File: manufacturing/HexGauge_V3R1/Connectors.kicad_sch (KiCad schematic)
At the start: 14 parts, among them J1 USB_B_Micro, J3 Micro_SD_Card, J4 Conn_01x04_Pin, J5 Conn_02x05_Odd_Even, U4 USBLC6-4

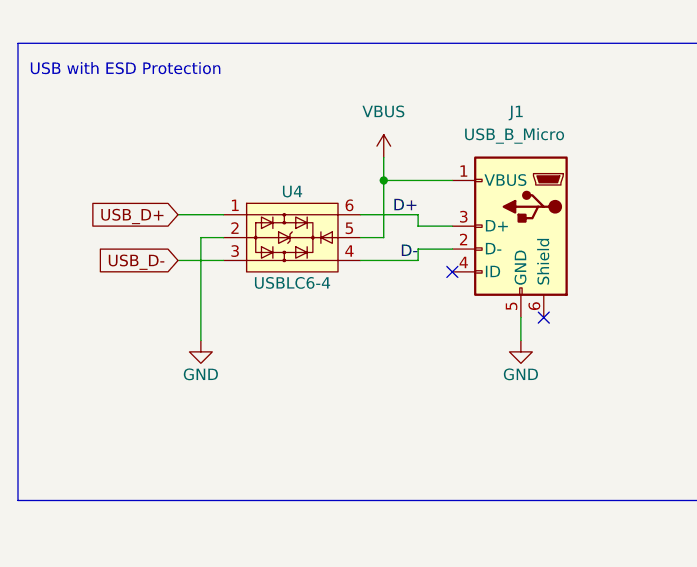
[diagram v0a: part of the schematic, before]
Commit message: Cost calculation
Find extended parts on mouser
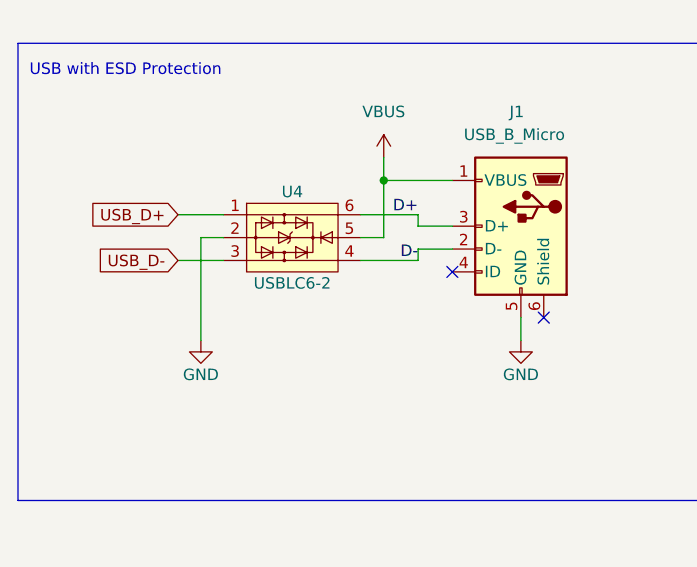
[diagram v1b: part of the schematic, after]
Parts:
- J5: footprint Connector_PinHeader_1.27mm:PinHeader_2x05_P1.27mm_Vertical_SMD -> Connector_PinHeader_1.27mm:PinHeader_2x05_P1.27mm_Vertical
- U4: value USBLC6-4 -> USBLC6-2; LCSC Part # C111212 -> C7519
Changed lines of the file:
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@@
       (effects (font (size 1.27 1.27)))
     )
-    (property "Footprint" "Connector_PinHeader_1.27mm:PinHeader_2x05_P1.27mm_Vertical_SMD" (at 137.16 63.5 0)
+    (property "Footprint" "Connector_PinHeader_1.27mm:PinHeader_2x05_P1.27mm_Vertical" (at 137.16 63.5 0)
       (effects (font (size 1.27 1.27)) hide)
     )
@@
     )
   )
+  (symbol (lib_id "Power_Protection:WE-TVS-82400102") (at 55.88 59.69 0) (unit 1)
+    (in_bom yes) (on_board yes) (dnp no)
+    (property "Reference" "U4" (at 55.88 54.61 0)
+      (effects (font (size 1.27 1.27)))
+    )
+    (property "Value" "USBLC6-2" (at 55.88 64.77 0)
+      (effects (font (size 1.27 1.27)))
+    )
+    (property "Footprint" "Package_TO_SOT_SMD:SOT-23-6" (at 55.88 64.77 0)
+      (effects (font (size 1.27 1.27)) hide)
+    )
+    (property "Datasheet" "https://www.st.com/resource/en/datasheet/usblc6-2.pdf" (at 55.88 66.04 0)
+      (effects (font (size 1.27 1.27)) hide)
+    )
+    (property "LCSC Part #" "C7519" (at 55.88 59.69 0)
+      (effects (font (size 1.27 1.27)) hide)
+    )
+    (pin "1")
+    (pin "2")
+    (pin "3")
+    (pin "4")
+    (pin "5")
+    (pin "6")
+    (instances
+      (project "STM32F4_HexGauge_V3"
+        (path "/1671c3d2-535f-4cd5-a65b-02e5c9ad18e5"
+          (reference "U4") (unit 1)
+        )
+        (path "/1671c3d2-535f-4cd5-a65b-02e5c9ad18e5/6132b015-8d81-4c9d-ab7f-afd3c7f45a00"
+          (reference "U6") (unit 1)
+        )
+        (path "/1671c3d2-535f-4cd5-a65b-02e5c9ad18e5/2ad56a2f-dfcc-4b7b-a763-7659f3fc7ffe"
+          (reference "U4") (unit 1)
+        )
+      )
+    )
+  )
   (symbol (lib_id "power:+3V3") (at 39.37 113.03 0) (unit 1)
     (in_bom yes) (on_board yes) (dnp no)
@@
         )
       )
-    )
-  )
-  (symbol (lib_id "Power_Protection:WE-TVS-82400102") (at 55.88 59.69 0) (unit 1)
-    (in_bom yes) (on_board yes) (dnp no)
-    (property "Reference" "U4" (at 55.88 54.61 0)
-      (effects (font (size 1.27 1.27)))
-    )
-    (property "Value" "USBLC6-4" (at 55.88 64.77 0)
-      (effects (font (size 1.27 1.27)))
-    )
-    (property "Footprint" "Package_TO_SOT_SMD:SOT-23-6" (at 55.88 64.77 0)
-      (effects (font (size 1.27 1.27)) hide)
-    )
-    (property "Datasheet" "https://katalog.we-online.de/pbs/datasheet/82400102.pdf" (at 55.88 66.04 0)
-      (effects (font (size 1.27 1.27)) hide)
-    )
-    (property "LCSC Part #" "C111212" (at 55.88 59.69 0)
-      (effects (font (size 1.27 1.27)) hide)
-    )
-    (pin "1")
-    (pin "2")
-    (pin "3")
-    (pin "4")
-    (pin "5")
-    (pin "6")
-    (instances
-      (project "STM32F4_HexGauge_V3"
-        (path "/1671c3d2-535f-4cd5-a65b-02e5c9ad18e5"
-          (reference "U4") (unit 1)
-        )
-        (path "/1671c3d2-535f-4cd5-a65b-02e5c9ad18e5/6132b015-8d81-4c9d-ab7f-afd3c7f45a00"
-          (reference "U6") (unit 1)
-        )
-      )
